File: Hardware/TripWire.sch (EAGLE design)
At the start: 56 parts, among them P1 LSP11, P2 LSP11, P3 LSP11, P4 LSP11, P5 LSP11, P6 LSP11, P7 LSP11, X1 GADGETEER-SOCKET

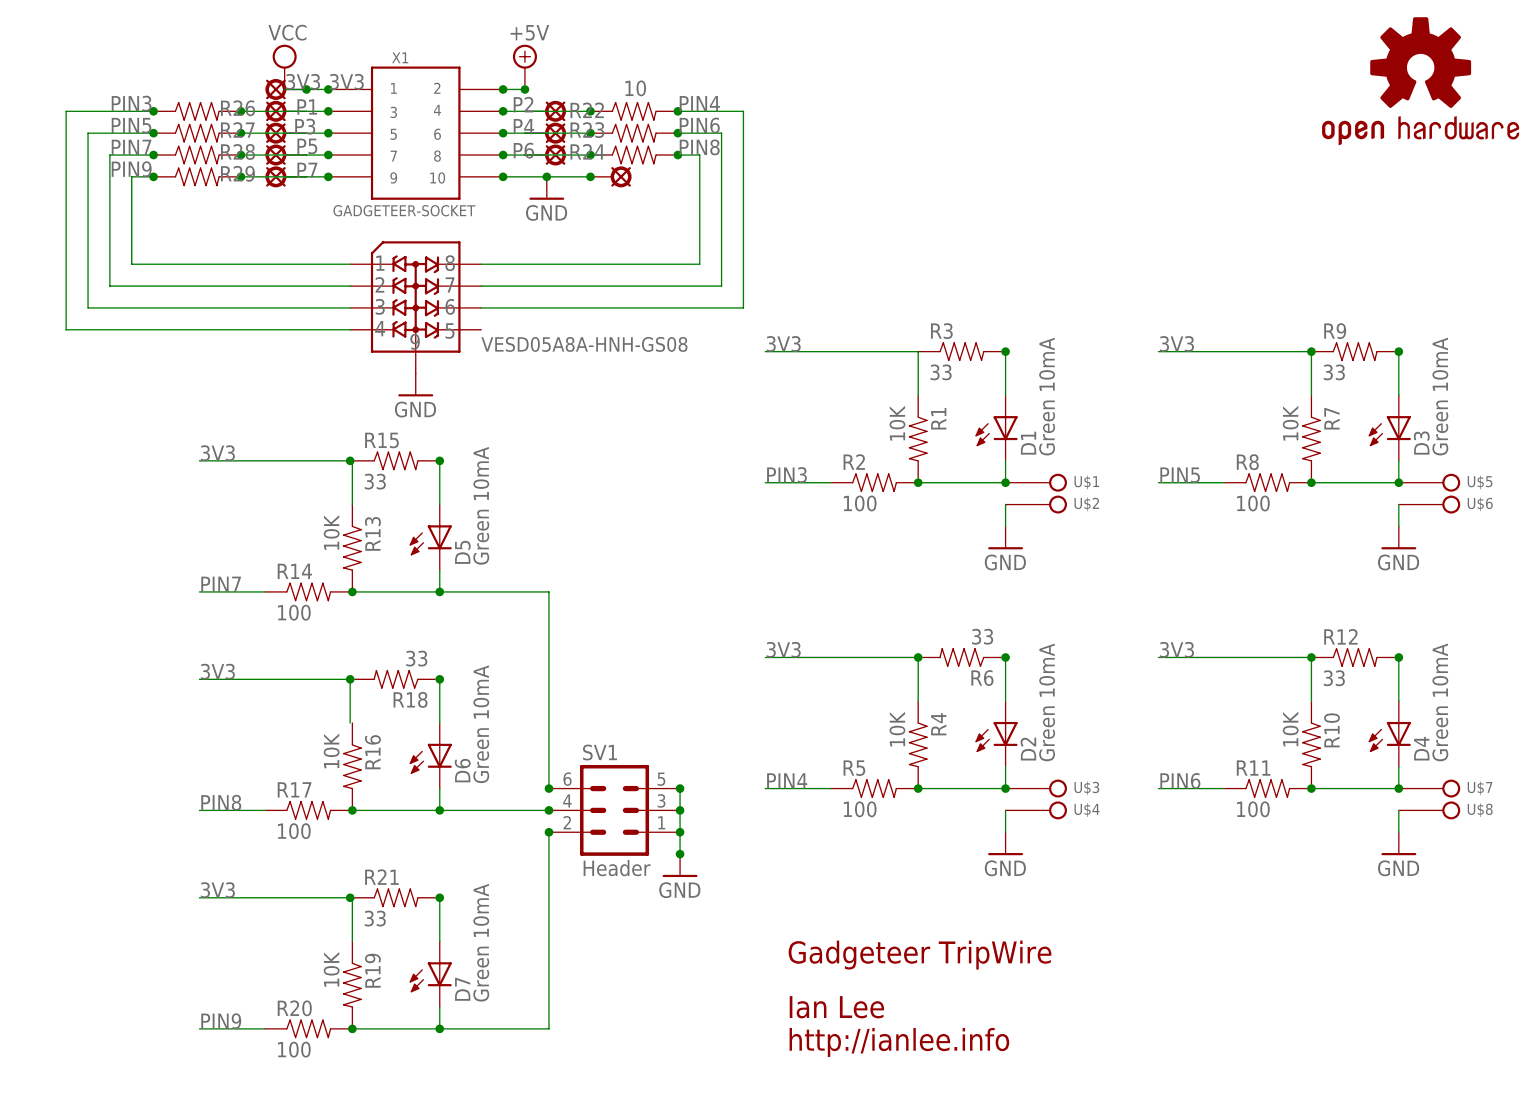
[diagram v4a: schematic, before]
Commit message: Started replacing TVS with BAT54S diode arrays.
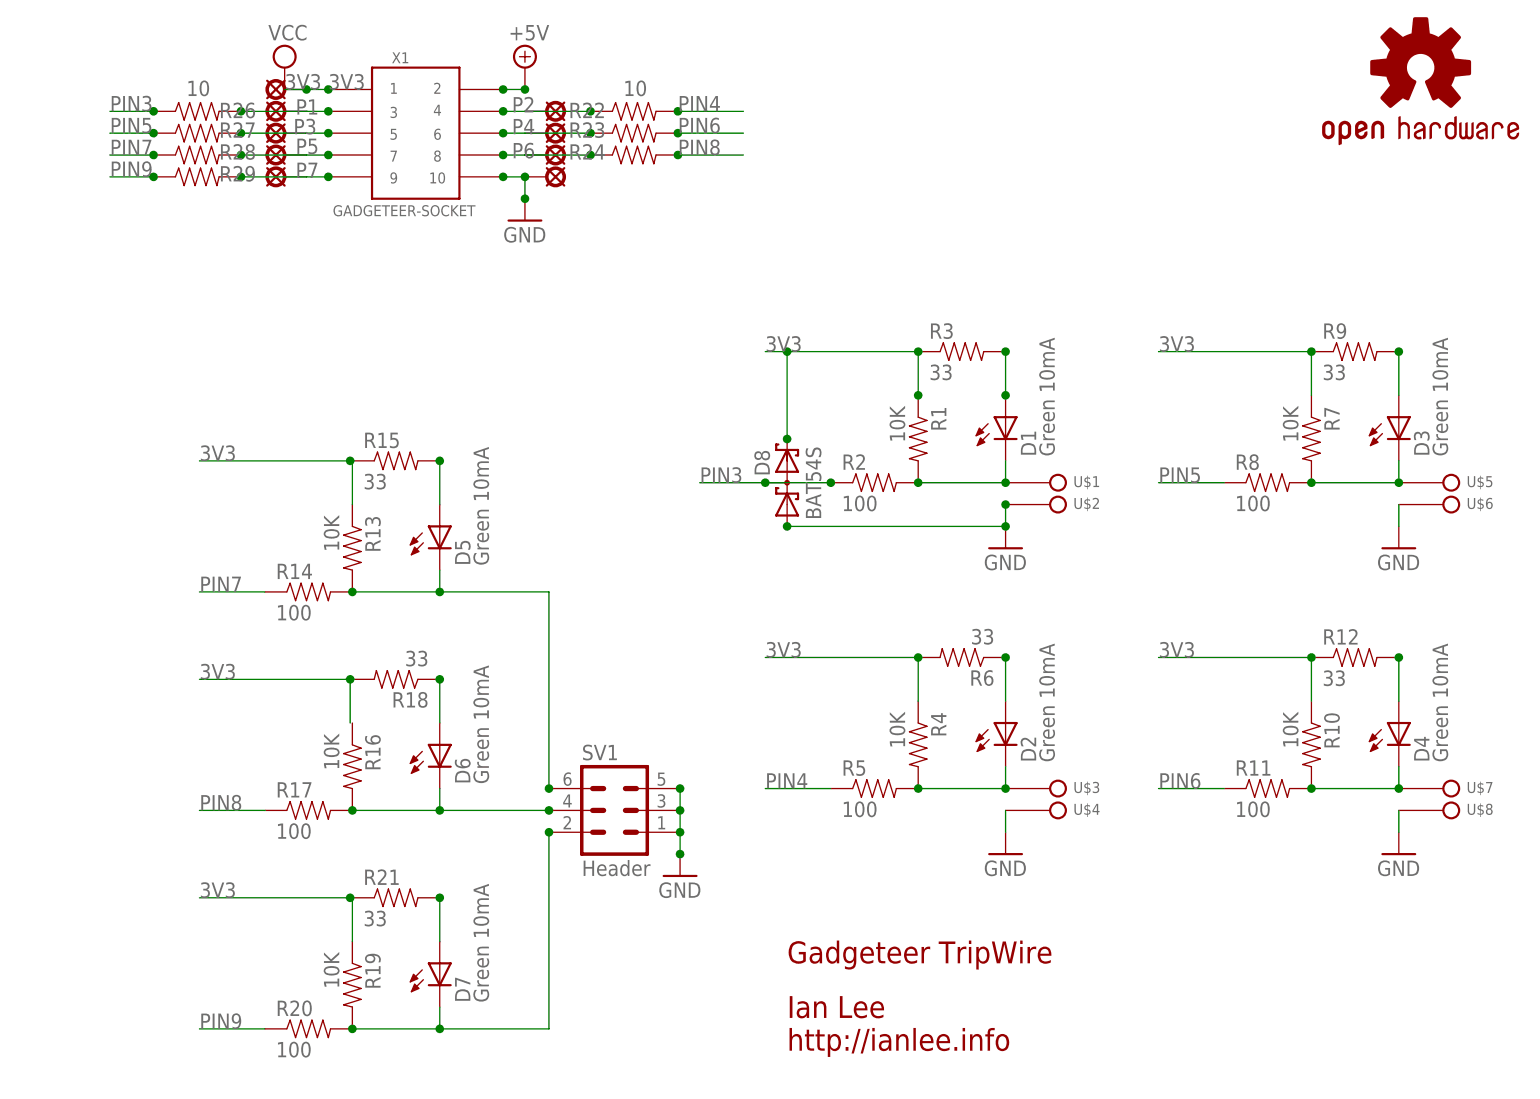
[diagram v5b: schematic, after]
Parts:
- removed VESD05A8A-HNH-GS08: VESD05A8A-HNH-GS088-UFDFN_TVS-DIODE-ARRAY, SoftDust:VESD05A8A-HNH-GS088-UFDFN_TVS-DIODE-ARRAY
- added D8: BAT54S, diode:BAT54S
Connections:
- net 3V3: now also D8.C2
- net GND: now also D8.A1; no longer VESD05A8A-HNH-GS08.P$9
- net PIN3: now also D8.C1A2; no longer VESD05A8A-HNH-GS08.P$4
- net PIN4: no longer VESD05A8A-HNH-GS08.P$6
- net PIN5: no longer VESD05A8A-HNH-GS08.P$3
- net PIN6: no longer VESD05A8A-HNH-GS08.P$7
- net PIN7: no longer VESD05A8A-HNH-GS08.P$2
- net PIN8: no longer VESD05A8A-HNH-GS08.P$8
- net PIN9: no longer VESD05A8A-HNH-GS08.P$1
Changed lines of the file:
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@@
 <setting verticaltext="up"/>
 </settings>
-<grid distance="0.1" unitdist="inch" unit="mm" style="lines" multiple="1" display="no" altdistance="0.01" altunitdist="inch" altunit="mm"/>
+<grid distance="0.1" unitdist="inch" unit="inch" style="lines" multiple="1" display="no" altdistance="0.01" altunitdist="inch" altunit="inch"/>
 <layers>
 <layer number="1" name="Top" color="4" fill="1" visible="no" active="no"/>
@@
 <part name="P5" library="solpad" deviceset="LSP11" device=""/>
 <part name="P7" library="solpad" deviceset="LSP11" device=""/>
-<part name="VESD05A8A-HNH-GS08" library="SoftDust" deviceset="VESD05A8A-HNH-GS08" device="8-UFDFN_TVS-DIODE-ARRAY"/>
-<part name="GND7" library="supply1" deviceset="GND" device=""/>
 <part name="SUPPLY1" library="supply2" deviceset="+5V" device=""/>
 <part name="LOGO1" library="SparkFun-Aesthetics" deviceset="OSHW-LOGO" device="M"/>
@@
 <part name="R28" library="SparkFun-Resistors" deviceset="RESISTOR" device="0603-RES" value="10"/>
 <part name="R29" library="SparkFun-Resistors" deviceset="RESISTOR" device="0603-RES" value="10"/>
+<part name="D8" library="diode" deviceset="BAT54S" device=""/>
 </parts>
 <sheets>
@@
 <instances>
 <instance part="FRAME2" gate="G$1" x="0" y="0"/>
-<instance part="GND1" gate="1" x="66.04" y="106.68"/>
+<instance part="GND1" gate="1" x="63.5" y="104.14"/>
 <instance part="V2" gate="G$1" x="35.56" y="121.92"/>
 <instance part="X1" gate="G$1" x="50.8" y="114.3" smashed="yes">
@@
 <attribute name="NAME" x="61.976" y="111.379" size="1.778" layer="95"/>
 </instance>
-<instance part="GND" gate="1" x="73.66" y="109.22" smashed="yes" rot="R270"/>
+<instance part="GND" gate="1" x="66.04" y="109.22" smashed="yes" rot="R270"/>
 <instance part="3V3" gate="1" x="35.56" y="119.38" smashed="yes" rot="R90"/>
 <instance part="P1" gate="1" x="35.56" y="116.84" smashed="yes" rot="R90">
@@
 <attribute name="NAME" x="36.83" y="109.093" size="1.778" layer="95"/>
 </instance>
-<instance part="VESD05A8A-HNH-GS08" gate="G$1" x="50.8" y="96.52" smashed="yes">
-<attribute name="NAME" x="58.42" y="88.9" size="1.6764" layer="95"/>
-</instance>
-<instance part="GND7" gate="1" x="50.8" y="83.82"/>
 <instance part="SUPPLY1" gate="+5V" x="63.5" y="121.92"/>
 <instance part="LOGO1" gate="G$1" x="167.64" y="121.92"/>
@@
 </instance>
 <instance part="R26" gate="G$1" x="25.4" y="116.84" smashed="yes">
-<attribute name="NAME" x="27.94" y="116.3066" size="1.778" layer="95"/>
+<attribute name="NAME" x="27.94" y="116.0526" size="1.778" layer="95"/>
+<attribute name="VALUE" x="24.13" y="118.618" size="1.778" layer="96"/>
 </instance>
 <instance part="R27" gate="G$1" x="25.4" y="114.3" smashed="yes">
@@
 <attribute name="NAME" x="27.94" y="108.6866" size="1.778" layer="95"/>
 </instance>
+<instance part="D8" gate="G$1" x="93.98" y="73.66" rot="R90"/>
 </instances>
 <busses>
@@
 <pinref part="R1" gate="G$1" pin="1"/>
 <wire x1="109.22" y1="83.82" x2="109.22" y2="88.9" width="0.1524" layer="91"/>
+<pinref part="R3" gate="G$1" pin="1"/>
+<wire x1="109.22" y1="88.9" x2="93.98" y2="88.9" width="0.1524" layer="91"/>
+<label x="91.44" y="88.9" size="1.778" layer="95"/>
+<pinref part="D8" gate="G$1" pin="C2"/>
+<wire x1="93.98" y1="88.9" x2="91.44" y2="88.9" width="0.1524" layer="91"/>
+<wire x1="93.98" y1="78.74" x2="93.98" y2="88.9" width="0.1524" layer="91"/>
+<junction x="93.98" y="88.9"/>
+<junction x="93.98" y="78.74"/>
+<junction x="109.22" y="88.9"/>
+<junction x="109.22" y="83.82"/>
 </segment>
 <segment>
@@
 <wire x1="43.18" y1="25.4" x2="25.654" y2="25.4" width="0.1524" layer="91"/>
 </segment>
-<segment>
-<pinref part="R3" gate="G$1" pin="1"/>
-<wire x1="109.22" y1="88.9" x2="91.44" y2="88.9" width="0.1524" layer="91"/>
-<label x="91.44" y="88.9" size="1.778" layer="95"/>
-</segment>
 </net>
 <net name="GND" class="1">
 <segment>
-<wire x1="66.04" y1="109.22" x2="60.96" y2="109.22" width="0.1524" layer="91"/>
 <pinref part="GND1" gate="1" pin="GND"/>
 <pinref part="X1" gate="G$1" pin="P$10"/>
 <pinref part="GND" gate="1" pin="MP"/>
-<wire x1="71.12" y1="109.22" x2="66.04" y2="109.22" width="0.1524" layer="91"/>
-<junction x="66.04" y="109.22"/>
-<junction x="71.12" y="109.22"/>
+<wire x1="63.5" y1="106.68" x2="63.5" y2="109.22" width="0.1524" layer="91"/>
+<wire x1="63.5" y1="109.22" x2="60.96" y2="109.22" width="0.1524" layer="91"/>
+<junction x="63.5" y="109.22"/>
 <junction x="60.96" y="109.22"/>
+<junction x="63.5" y="106.68"/>
 </segment>
 <segment>
@@
 <pinref part="GND2" gate="1" pin="GND"/>
 <wire x1="119.38" y1="68.58" x2="119.38" y2="71.12" width="0.1524" layer="91"/>
+<pinref part="D8" gate="G$1" pin="A1"/>
+<wire x1="93.98" y1="68.58" x2="119.38" y2="68.58" width="0.1524" layer="91"/>
+<junction x="93.98" y="68.58"/>
+<junction x="119.38" y="68.58"/>
+<junction x="119.38" y="71.12"/>
 </segment>
 <segment>
@@
 <junction x="81.534" y="30.48"/>
 </segment>
-<segment>
-<pinref part="GND7" gate="1" pin="GND"/>
-<pinref part="VESD05A8A-HNH-GS08" gate="G$1" pin="P$9"/>
-</segment>
 </net>
 <net name="PIN3" class="0">
 <segment>
-<wire x1="10.16" y1="91.44" x2="43.18" y2="91.44" width="0.1524" layer="91"/>
-<pinref part="VESD05A8A-HNH-GS08" gate="G$1" pin="P$4"/>
-<wire x1="10.16" y1="91.44" x2="10.16" y2="116.84" width="0.1524" layer="91"/>
 <pinref part="R26" gate="G$1" pin="1"/>
-<wire x1="10.16" y1="116.84" x2="20.32" y2="116.84" width="0.1524" layer="91"/>
+<wire x1="15.24" y1="116.84" x2="20.32" y2="116.84" width="0.1524" layer="91"/>
 <junction x="20.32" y="116.84"/>
 <label x="15.24" y="116.84" size="1.778" layer="95"/>
@@
 <segment>
 <pinref part="R2" gate="G$1" pin="1"/>
-<label x="91.44" y="73.66" size="1.778" layer="95"/>
+<label x="83.82" y="73.66" size="1.778" layer="95"/>
 <wire x1="99.06" y1="73.66" x2="91.44" y2="73.66" width="0.1524" layer="91"/>
+<pinref part="D8" gate="G$1" pin="C1A2"/>
+<junction x="91.44" y="73.66"/>
+<wire x1="91.44" y1="73.66" x2="83.82" y2="73.66" width="0.1524" layer="91"/>
+<junction x="99.06" y="73.66"/>
 </segment>
 </net>
@@
 <segment>
 <label x="81.28" y="116.84" size="1.778" layer="95"/>
-<wire x1="88.9" y1="93.98" x2="58.42" y2="93.98" width="0.1524" layer="91"/>
-<pinref part="VESD05A8A-HNH-GS08" gate="G$1" pin="P$6"/>
-<wire x1="88.9" y1="93.98" x2="88.9" y2="116.84" width="0.1524" layer="91"/>
 <pinref part="R22" gate="G$1" pin="2"/>
 <wire x1="88.9" y1="116.84" x2="81.28" y2="116.84" width="0.1524" layer="91"/>
@@
 <net name="PIN5" class="0">
 <segment>
-<wire x1="12.7" y1="93.98" x2="43.18" y2="93.98" width="0.1524" layer="91"/>
-<pinref part="VESD05A8A-HNH-GS08" gate="G$1" pin="P$3"/>
-<wire x1="12.7" y1="93.98" x2="12.7" y2="114.3" width="0.1524" layer="91"/>
-<wire x1="12.7" y1="114.3" x2="20.32" y2="114.3" width="0.1524" layer="91"/>
+<wire x1="15.24" y1="114.3" x2="20.32" y2="114.3" width="0.1524" layer="91"/>
 <pinref part="R27" gate="G$1" pin="1"/>
 <junction x="20.32" y="114.3"/>
@@
 <net name="PIN7" class="0">
 <segment>
-<wire x1="15.24" y1="96.52" x2="43.18" y2="96.52" width="0.1524" layer="91"/>
-<pinref part="VESD05A8A-HNH-GS08" gate="G$1" pin="P$2"/>
-<wire x1="15.24" y1="96.52" x2="15.24" y2="111.76" width="0.1524" layer="91"/>
 <pinref part="R28" gate="G$1" pin="1"/>
 <wire x1="15.24" y1="111.76" x2="20.32" y2="111.76" width="0.1524" layer="91"/>
@@
 <net name="PIN9" class="0">
 <segment>
-<pinref part="VESD05A8A-HNH-GS08" gate="G$1" pin="P$1"/>
-<wire x1="43.18" y1="99.06" x2="17.78" y2="99.06" width="0.1524" layer="91"/>
-<wire x1="17.78" y1="99.06" x2="17.78" y2="109.22" width="0.1524" layer="91"/>
 <pinref part="R29" gate="G$1" pin="1"/>
-<wire x1="17.78" y1="109.22" x2="20.32" y2="109.22" width="0.1524" layer="91"/>
+<wire x1="15.24" y1="109.22" x2="20.32" y2="109.22" width="0.1524" layer="91"/>
 <junction x="20.32" y="109.22"/>
 <label x="15.24" y="109.22" size="1.778" layer="95"/>
@@
 <segment>
 <label x="81.28" y="114.3" size="1.778" layer="95"/>
-<wire x1="86.36" y1="96.52" x2="58.42" y2="96.52" width="0.1524" layer="91"/>
-<pinref part="VESD05A8A-HNH-GS08" gate="G$1" pin="P$7"/>
-<wire x1="86.36" y1="96.52" x2="86.36" y2="114.3" width="0.1524" layer="91"/>
 <pinref part="R23" gate="G$1" pin="2"/>
-<wire x1="86.36" y1="114.3" x2="81.28" y2="114.3" width="0.1524" layer="91"/>
+<wire x1="88.9" y1="114.3" x2="81.28" y2="114.3" width="0.1524" layer="91"/>
 <junction x="81.28" y="114.3"/>
 </segment>
@@
 <segment>
 <label x="81.28" y="111.76" size="1.778" layer="95"/>
-<wire x1="83.82" y1="99.06" x2="58.42" y2="99.06" width="0.1524" layer="91"/>
-<pinref part="VESD05A8A-HNH-GS08" gate="G$1" pin="P$8"/>
-<wire x1="83.82" y1="99.06" x2="83.82" y2="111.76" width="0.1524" layer="91"/>
 <pinref part="R24" gate="G$1" pin="2"/>
-<wire x1="83.82" y1="111.76" x2="81.28" y2="111.76" width="0.1524" layer="91"/>
+<wire x1="88.9" y1="111.76" x2="81.28" y2="111.76" width="0.1524" layer="91"/>
 <junction x="81.28" y="111.76"/>
 </segment>
@@
 <wire x1="119.38" y1="88.9" x2="119.38" y2="83.82" width="0.1524" layer="91"/>
 <junction x="119.38" y="88.9"/>
-</segment>
-</net>
+<junction x="119.38" y="83.82"/>
+</segment>
+</net>

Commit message: Downgraded to Eagle 6.1.0.  Added Schottky circuit protection and signal filtering capacitors.
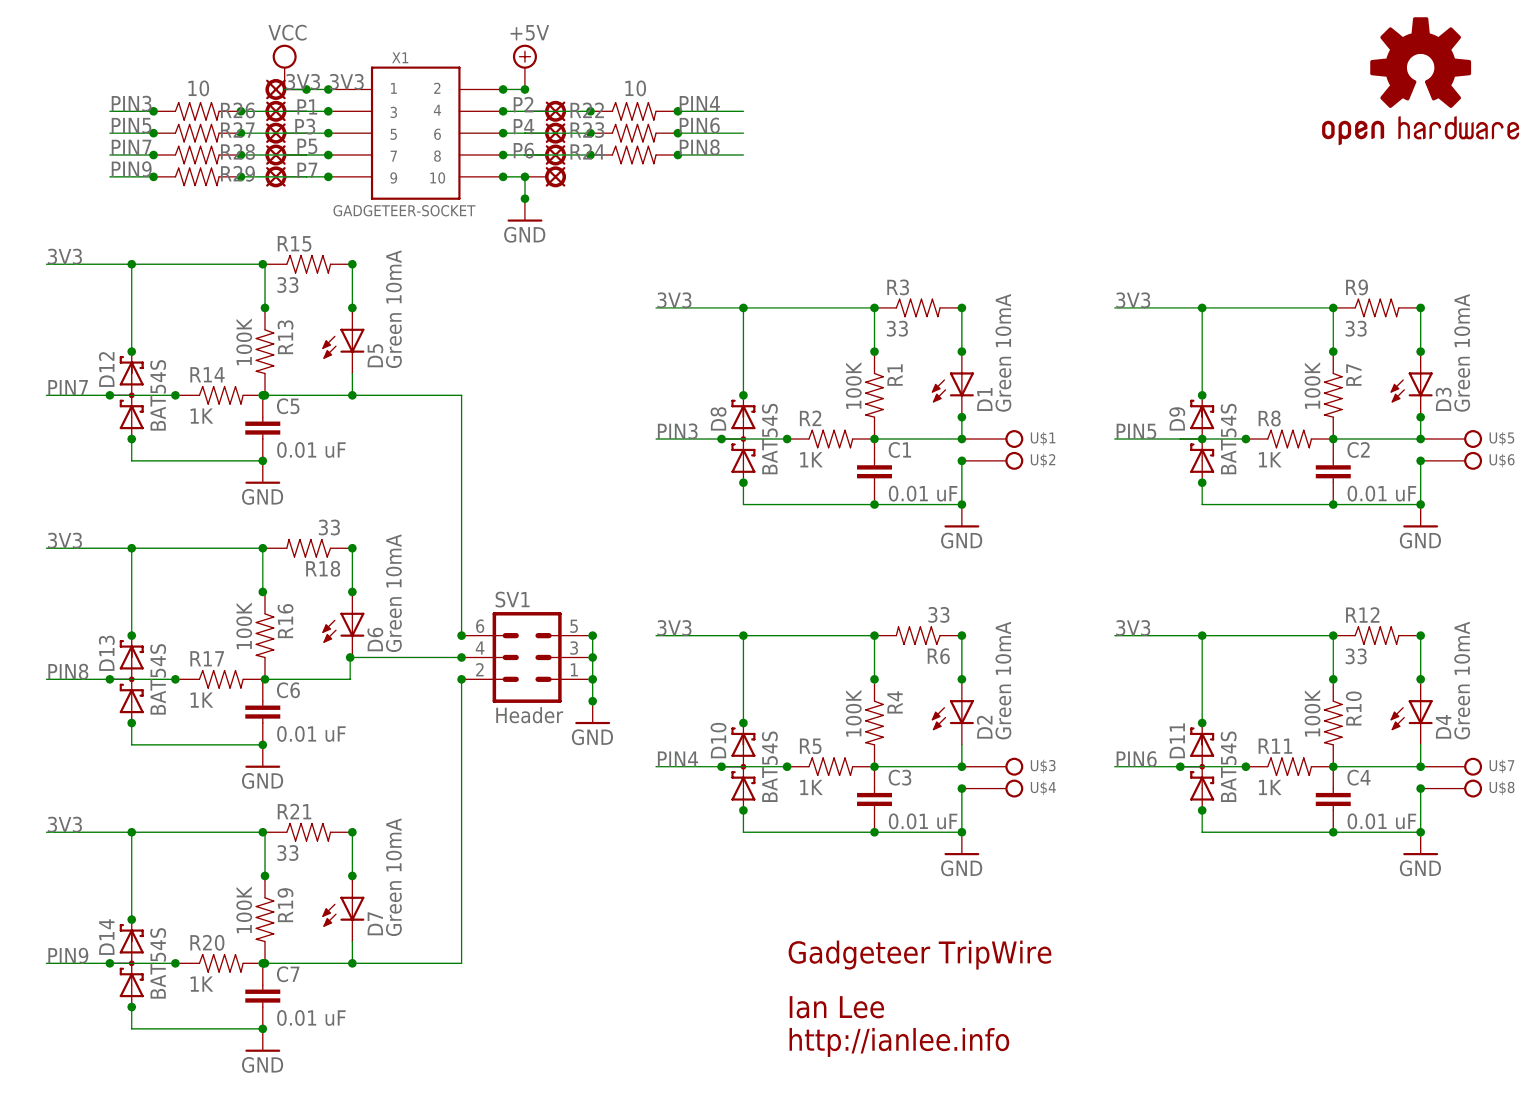
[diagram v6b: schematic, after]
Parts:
- added C1, C2, C3, C4, C5, C6, C7: 0.01 uF, SparkFun-Capacitors:CAP0603-CAP
- added D10, D11, D12, D13, D14, D9: BAT54S, diode:BAT54S
- R1, R10, R13, R16, R19, R4, R7: value 10K -> 100K
- R11, R14, R17, R2, R20, R5, R8: value 100 -> 1K
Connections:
- new net N$23: C6.1, R16.2, R17.2
- net 3V3: now also D10.C2, D11.C2, D12.C2, D13.C2, D14.C2, D9.C2
- net GND: now also C1.2, C2.2, C3.2, C4.2, C5.2, C6.2, C7.2, D10.A1, D11.A1, D12.A1, D13.A1, D14.A1, D9.A1
- net N$11: now also C1.1
- net N$14: now also C5.1
- net N$2: now also C3.1
- net N$4: now also C2.1
- net N$6: now also C7.1
- net N$8: now also C4.1
- net N$9: no longer R16.2, R17.2
- net PIN4: now also D10.C1A2
- net PIN5: now also D9.C1A2
- net PIN6: now also D11.C1A2
- net PIN7: now also D12.C1A2
- net PIN8: now also D13.C1A2
- net PIN9: now also D14.C1A2
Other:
- moved on the sheet: D1, D2, D3, D4, D5, D6, D7, D8, R1, R10, R11, R12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
